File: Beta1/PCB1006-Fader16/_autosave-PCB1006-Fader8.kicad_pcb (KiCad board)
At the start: 2 copper layers, 155 x 62 mm, 43 parts, among them U1000 MCP3008T-I/SL

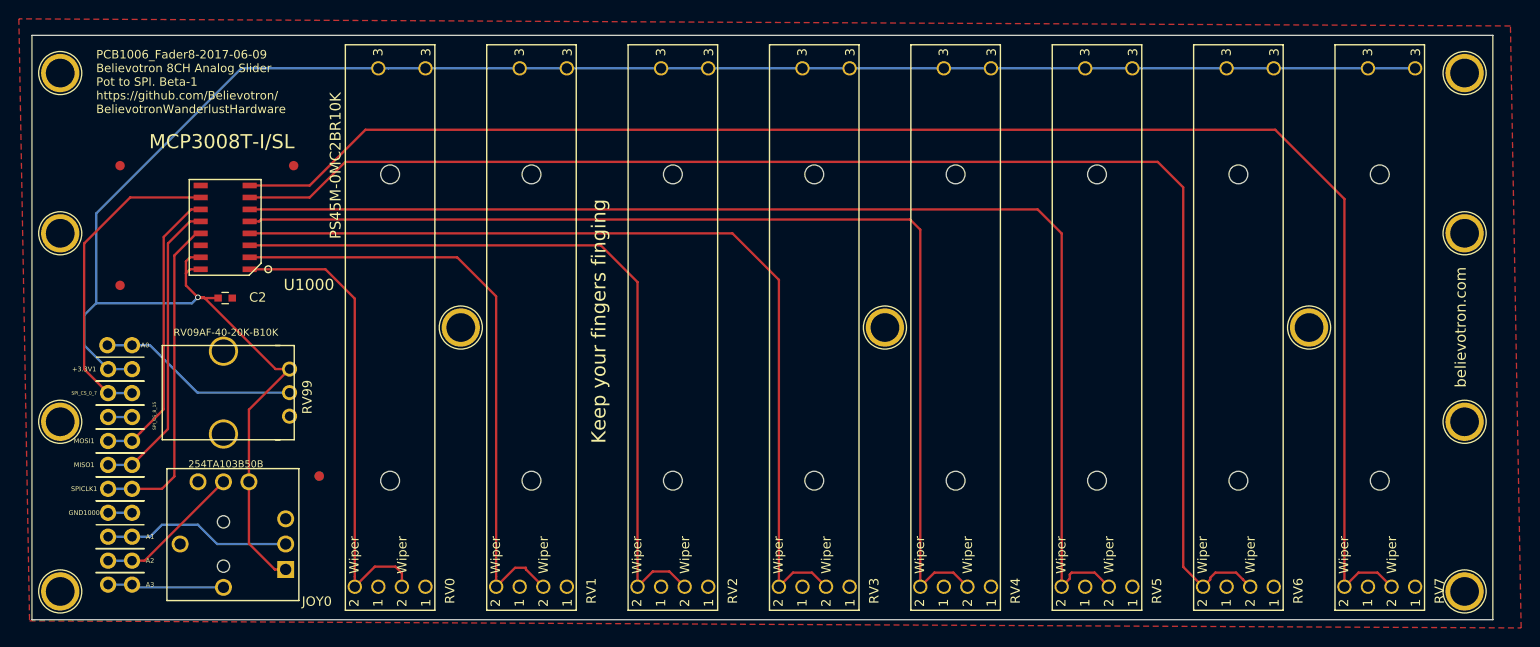
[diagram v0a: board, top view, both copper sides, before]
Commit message: Changed mounting holes to add DIN rail support.
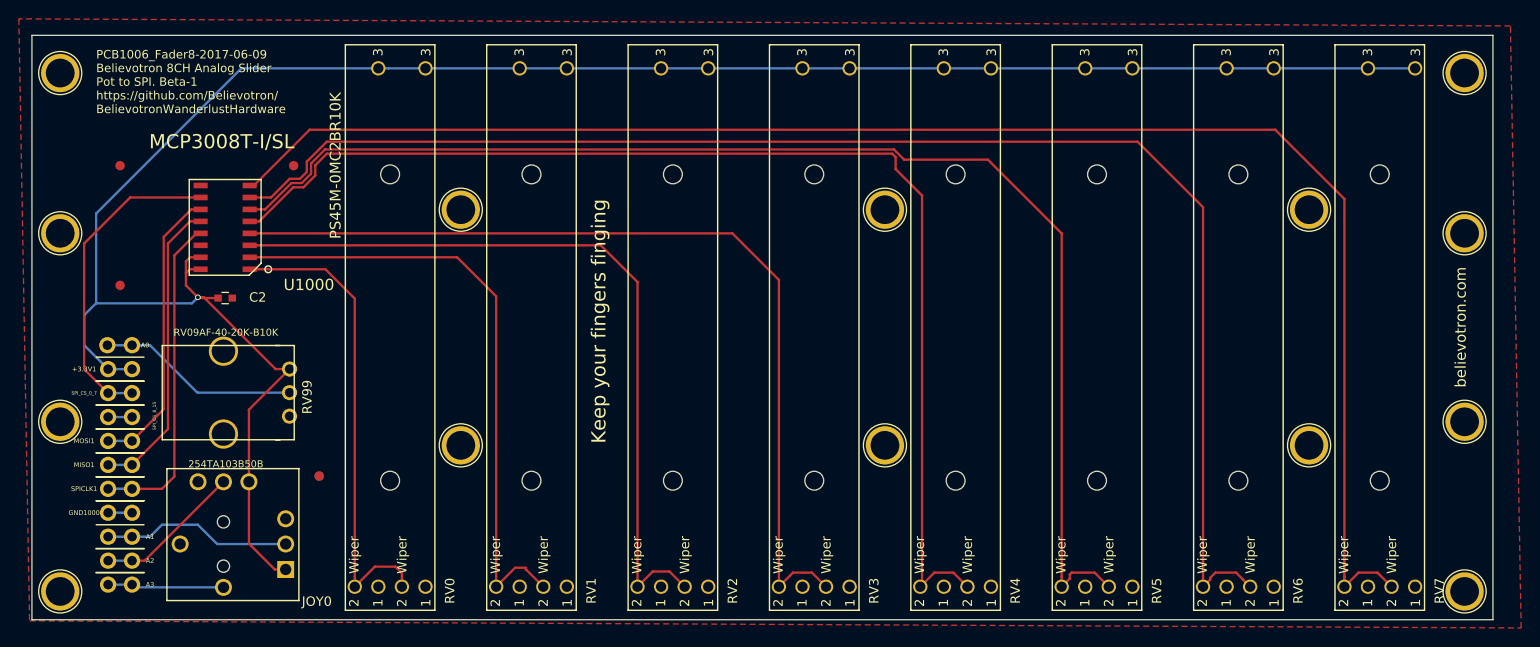
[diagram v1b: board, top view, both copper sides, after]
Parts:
- added REF**: 1pin, Connect:1pin, F.Cu at (135.5, -18.5)
- added REF**: 1pin, Connect:1pin, F.Cu at (90.5, -18.5)
- added REF**: 1pin, Connect:1pin, F.Cu at (45.5, -18.5)
- moved REF** 12.5 mm to (135.5, -43.5)
- moved REF** 12.5 mm to (45.5, -43.5)
- moved REF** 12.5 mm to (90.5, -43.5)
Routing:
- net /P4: track 115.8 -> 125.4 mm
- net /P5: track 131.2 -> 137.1 mm
- net /P6: track 151.3 -> 153.7 mm
